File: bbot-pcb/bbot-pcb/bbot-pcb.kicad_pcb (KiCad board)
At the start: 2 copper layers, 9 parts, among them U1 HA-552-4P, U10 L293D, U2 HMC5883L, U3 HA-552-4P, U4 ArduinoProMicro, U5 L7805, U6 Screw_Terminal_2, U7 74HC595, U9 L293D

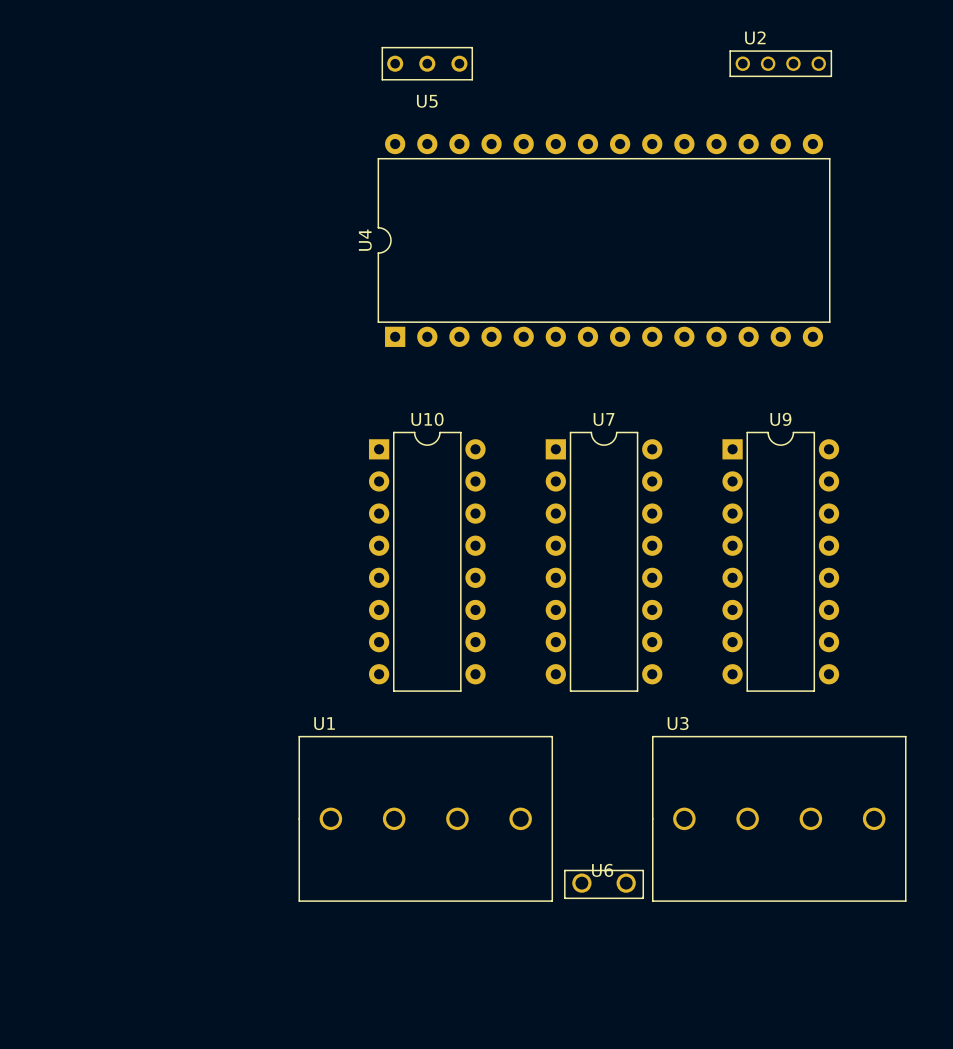
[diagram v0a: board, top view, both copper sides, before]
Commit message: unverified prototype of completed circuit board design. not quite ready to ship off to a fab yet
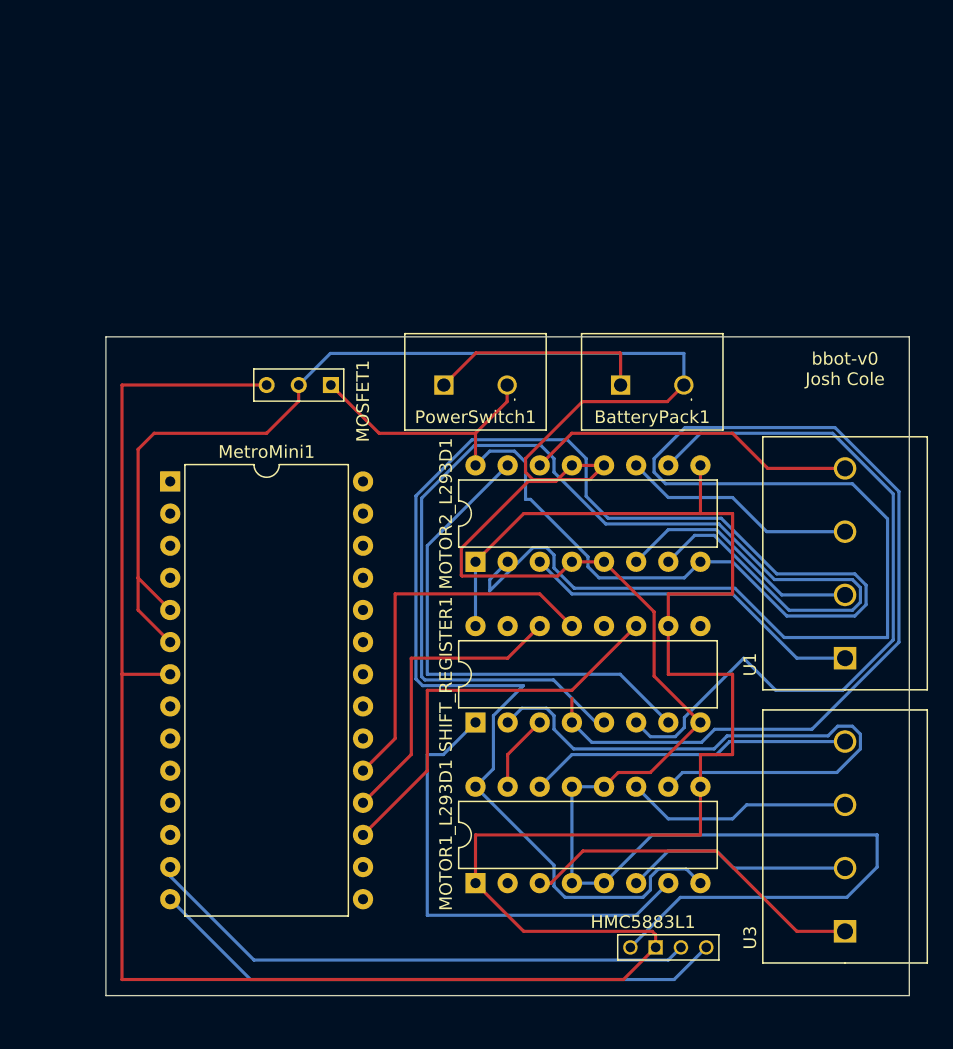
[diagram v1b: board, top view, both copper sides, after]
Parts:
- removed U10, U9: L293D, Package_DIP:DIP-16_W7.62mm
- removed U2: HMC5883L, bbot-pcb:HMC588L
- removed U4: ArduinoProMicro, Package_DIP:DIP-28_W15.24mm
- removed U5: L7805, bbot-pcb:L7805-A
- removed U6: Screw_Terminal_2, bbot-pcb:Screw_Terminal_2
- removed U7: 74HC595, Package_DIP:DIP-16_W7.62mm
- added BatteryPack1: Screw_Terminal_2, bbot-pcb:Screw_Terminal_2, F.Cu at (161.3, 62.2)
- added HMC5883L1: HMC5883L, bbot-pcb:HMC588L, F.Cu at (162.6, 106.7)
- added MOSFET1: L7805, bbot-pcb:L7805-A, F.Cu at (133.3, 62.2)
- added MOTOR1_L293D1: L293D, Package_DIP:DIP-16_W7.62mm, F.Cu at (147.3, 101.6)
- added MOTOR2_L293D1: L293D, Package_DIP:DIP-16_W7.62mm, F.Cu at (147.3, 76.2)
- added MetroMini1: MetroMini, Package_DIP:DIP-28_W15.24mm, F.Cu at (123.2, 69.8)
- added PowerSwitch1: Screw_Terminal_2, bbot-pcb:Screw_Terminal_2, F.Cu at (147.3, 62.2)
- added SHIFT_REGISTER1: 74HC595, Package_DIP:DIP-16_W7.62mm, F.Cu at (147.3, 88.9)
- moved U1 42.6 mm to (176.5, 83.8), turned to 90 degrees
- moved U3 15.5 mm to (176.5, 105.4), turned to 90 degrees
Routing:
- net 5V: track 0.00 -> 212.9 mm
- net GND: track 0.00 -> 206.4 mm
- net /12V: track 0.00 -> 163.3 mm
- net /MOTOR2_A: track 0.00 -> 135.8 mm
- net /MOTOR2_B: track 0.00 -> 91.6 mm
- net /MOTOR2_C: track 0.00 -> 58.9 mm
- net /MOTOR1_C: track 0.00 -> 48.9 mm
- net SCL: track 0.00 -> 46.1 mm
- net SDA: track 0.00 -> 44.3 mm
- net /MOTOR2_D: track 0.00 -> 39.8 mm
- net /MOTOR1_B: track 0.00 -> 37.7 mm
- net SHIFT_CLCK: track 0.00 -> 32.1 mm
- net SHIFT_LATCH: track 0.00 -> 30.0 mm
- net /MOTOR1_PHASE_A: track 0.00 -> 27.8 mm
- net /MOTOR2_PHASE_A: track 0.00 -> 27.3 mm
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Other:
- board outline added: 63.5 x 52.1 mm
- board text added: "bbot-v0 Josh Cole"

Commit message: finalize kicad circuit board.
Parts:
- added REF**: MountingHole_3.2mm_M3, MountingHole:MountingHole_3.2mm_M3, F.Cu at (146.1, 62.2)
- moved PowerSwitch1 48.9 mm to (127.0, 106.7), turned to 180 degrees
- moved BatteryPack1 47.4 mm to (144.8, 106.7), turned to 180 degrees
- moved MOSFET1 47.4 mm to (116.8, 106.7), turned to 270 degrees
- moved HMC5883L1 47.2 mm to (116.8, 95.0), turned to 270 degrees
- moved U1 21.9 mm to (172.7, 62.2), turned to 180 degrees
- moved MOTOR1_L293D1 11.7 mm to (156.2, 94.0)
- moved MOTOR2_L293D1 9.67 mm to (156.2, 80.0)
- moved MetroMini1 5.24 mm to (121.9, 64.8)
- moved SHIFT_REGISTER1 2.84 mm to (149.9, 90.2), turned to 180 degrees
- moved U3 2.84 mm to (174.0, 104.1), turned to 180 degrees
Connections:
- MOTOR1_L293D1 pad 12: GND -> Net-(MOTOR1_L293D1-Pad12)
- MOTOR1_L293D1 pad 13: GND -> Net-(MOTOR1_L293D1-Pad13)
- MOTOR1_L293D1 pad 4: GND -> Net-(MOTOR1_L293D1-Pad4)
- MOTOR2_L293D1 pad 13: GND -> Net-(MOTOR2_L293D1-Pad13)
- MOTOR2_L293D1 pad 4: GND -> Net-(MOTOR2_L293D1-Pad4)
- MOTOR2_L293D1 pad 5: GND -> Net-(MOTOR2_L293D1-Pad5)
- SHIFT_REGISTER1 pad 12: Net-(SHIFT_REGISTER1-Pad12) -> SHIFT_LATCH
- SHIFT_REGISTER1 pad 13: SHIFT_LATCH -> GND
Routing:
- net /MOTOR2_A: track 135.8 -> 24.9 mm
- net /MOTOR2_B: track 91.6 -> 23.7 mm
- net GND: track 206.4 -> 158.9 mm
- net SCL: track 46.1 -> 5.16 mm
- net SDA: track 44.3 -> 5.38 mm
- net /12V: track 163.3 -> 130.8 mm
- net /MOTOR2_D: track 39.8 -> 13.9 mm
- net /MOTOR1_C: track 48.9 -> 24.7 mm
- net SHIFT_LATCH: track 30.0 -> 9.72 mm
- net /MOTOR1_A: track 0.00 -> 19.1 mm
- net SHIFT_DATA: track 24.2 -> 7.18 mm
- net 5V: track 212.9 -> 197.6 mm
- net /MOTOR2_PHASE_D: track 26.3 -> 11.6 mm
- net SHIFT_CLCK: track 32.1 -> 21.0 mm
- net /MOTOR2_PHASE_A: track 27.3 -> 37.0 mm
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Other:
- board size 63.5 x 52.1 mm -> 66 x 54.6 mm
- board text added: "Battery Pack"
- board text added: "Power Switch"
- board text added: "a robot"
- board text added: "is this enough?"
- board text added: "lol"
